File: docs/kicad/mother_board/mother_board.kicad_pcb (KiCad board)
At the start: 2 copper layers, 148 x 93 mm, 32 parts, among them J1 ROW_BOARDS, J10 PEDAL1, J11 PEDAL2, J12 PEDAL3, J13 PEDAL4, J14 GUITAR_IN, J15 LINE_OUT, J16 LEDS, J2 ROTARIES, J3 TE_DISPLAY, J4 RPI_DISPLAY, J5 rPi_5V, J6 RPI_RUN, J7 rpi_connector, J8 I2S_TXB, J9 EigthInchJack1, Q1 BC547, U1 teensyAudioRevD_WithAudio, U2 myTeensy4.1

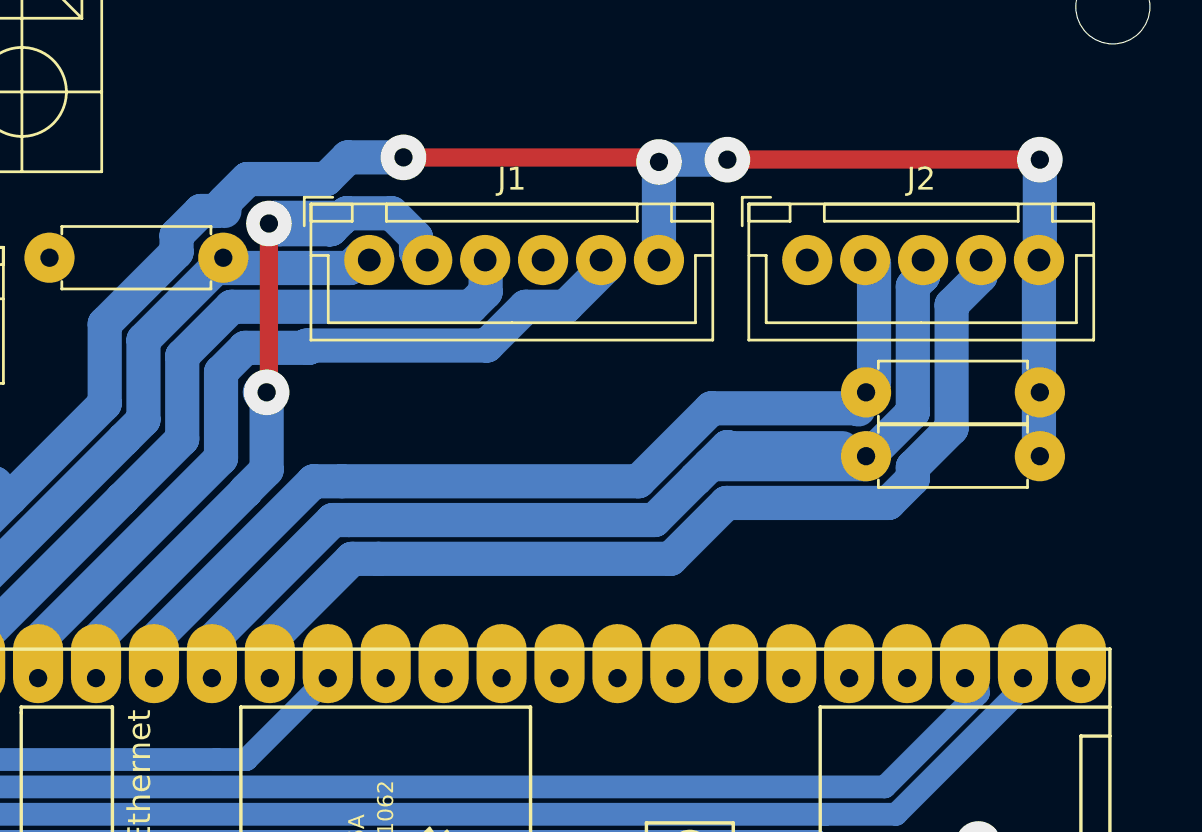
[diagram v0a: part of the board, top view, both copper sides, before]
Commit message: kicad changes to support actual Fusion 360 TE3 design efforts - created rotary board PCB
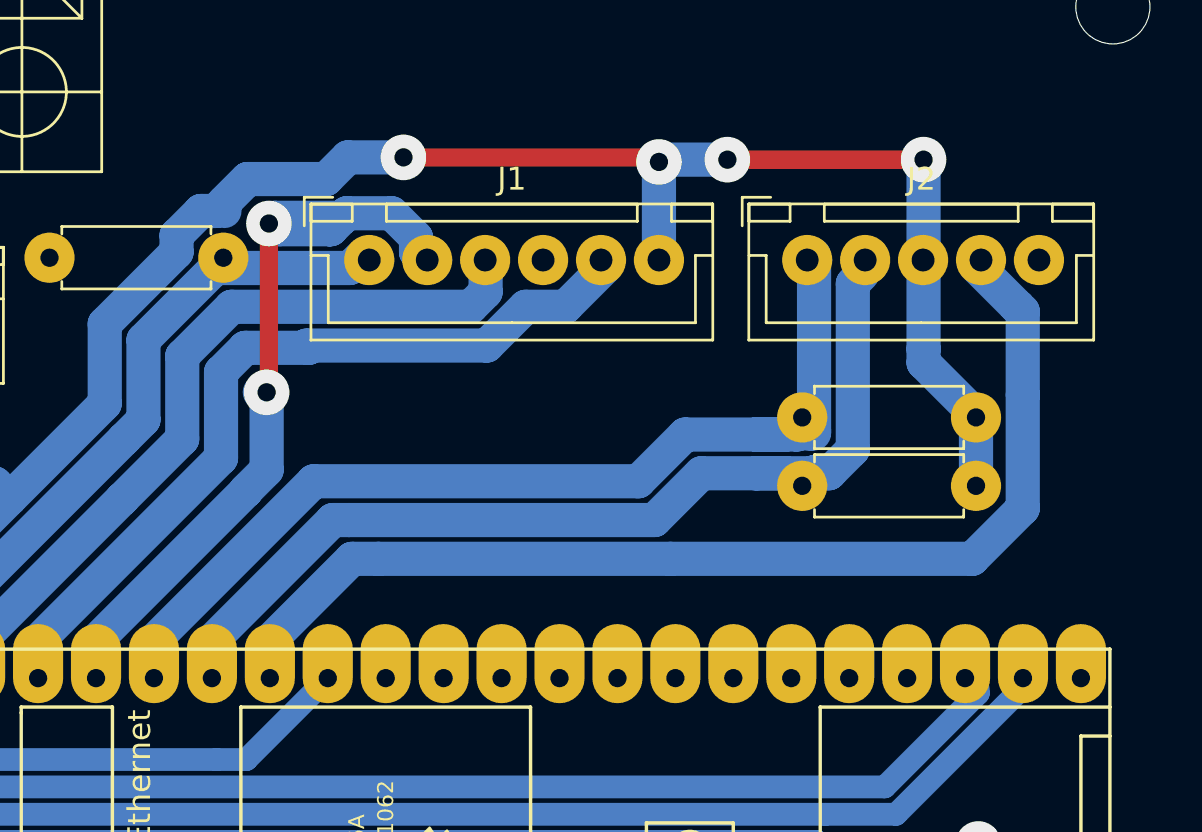
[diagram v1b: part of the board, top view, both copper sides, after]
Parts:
- moved R2 3.09 mm to (202.0, 84.0)
- moved R1 3.01 mm to (202.0, 81.0)
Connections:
- J2 pad 1: GND -> T41_SCL
- J2 pad 2: T41_SCL -> T41_SDA
- J2 pad 3: T41_SDA -> T41_3V3
- J2 pad 5: T41_3V3 -> GND
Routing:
- net ROT_INT: track 43.6 -> 51.1 mm
- net T41_SDA: track 50.3 -> 43.9 mm
- net T41_3V3: track 109.8 -> 107.0 mm
- net T41_SCL: track 42.6 -> 45.1 mm

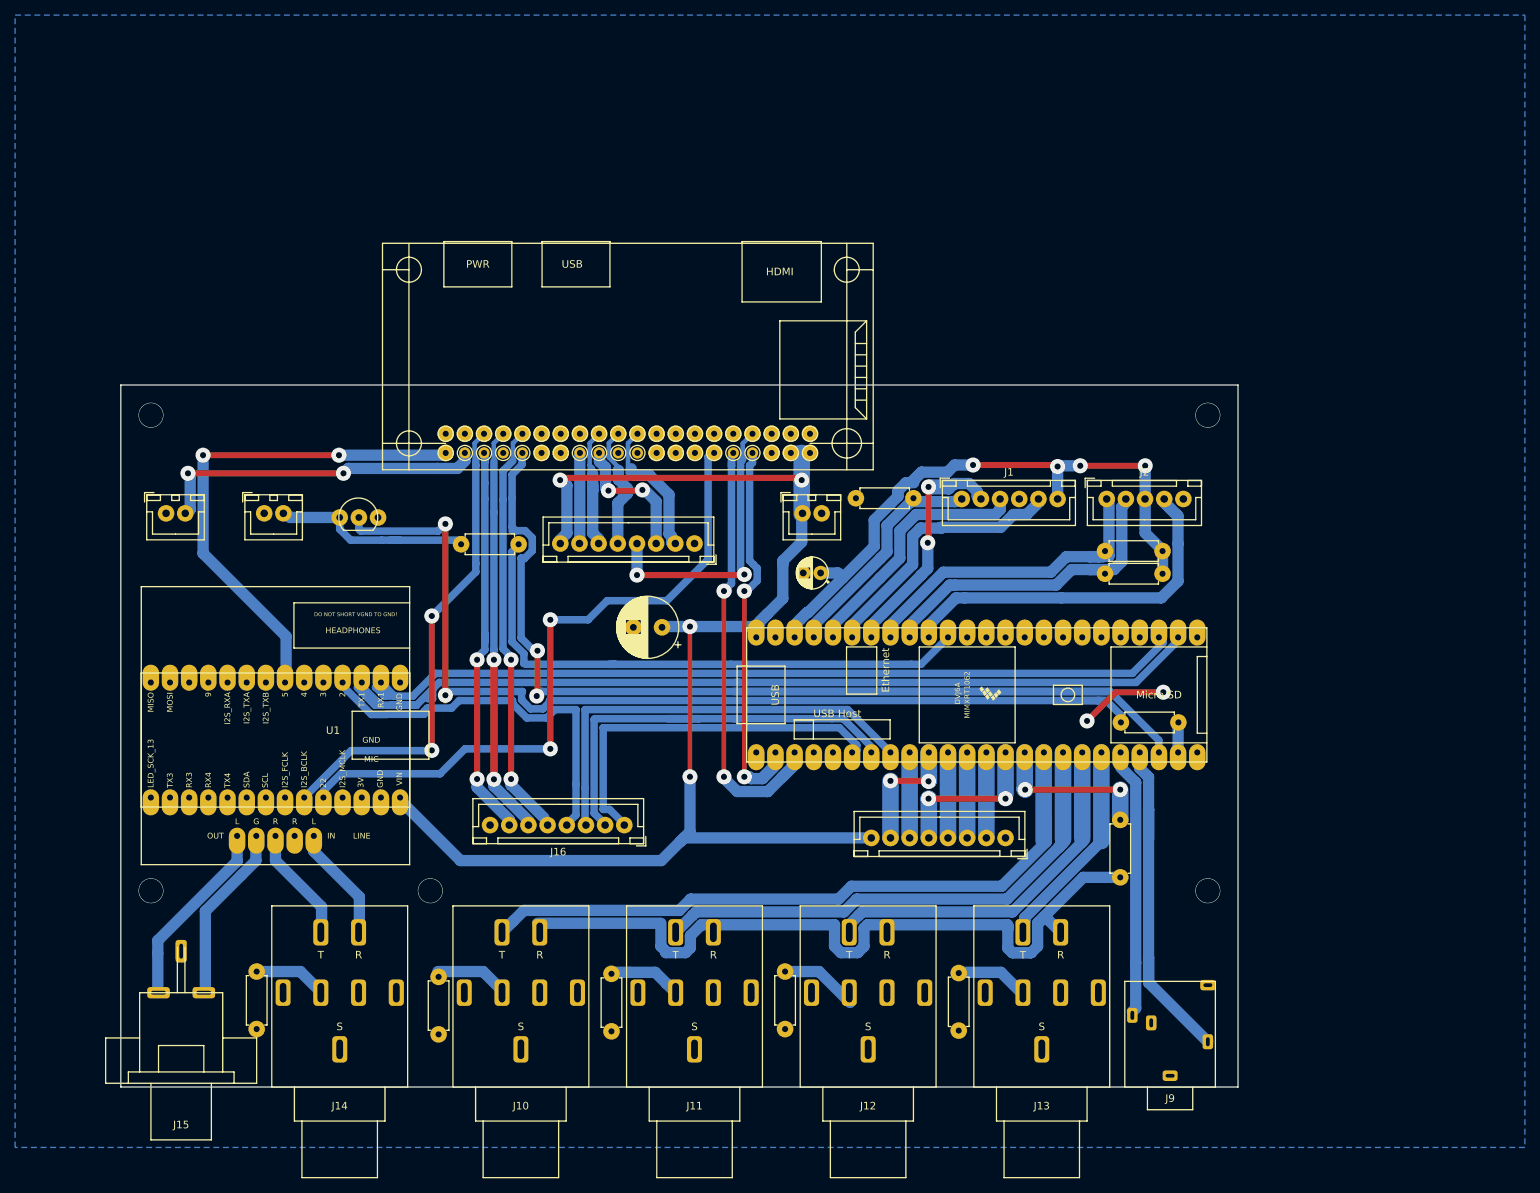
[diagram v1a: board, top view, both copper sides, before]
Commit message: added kicad led_board, updated mother board RCA socket
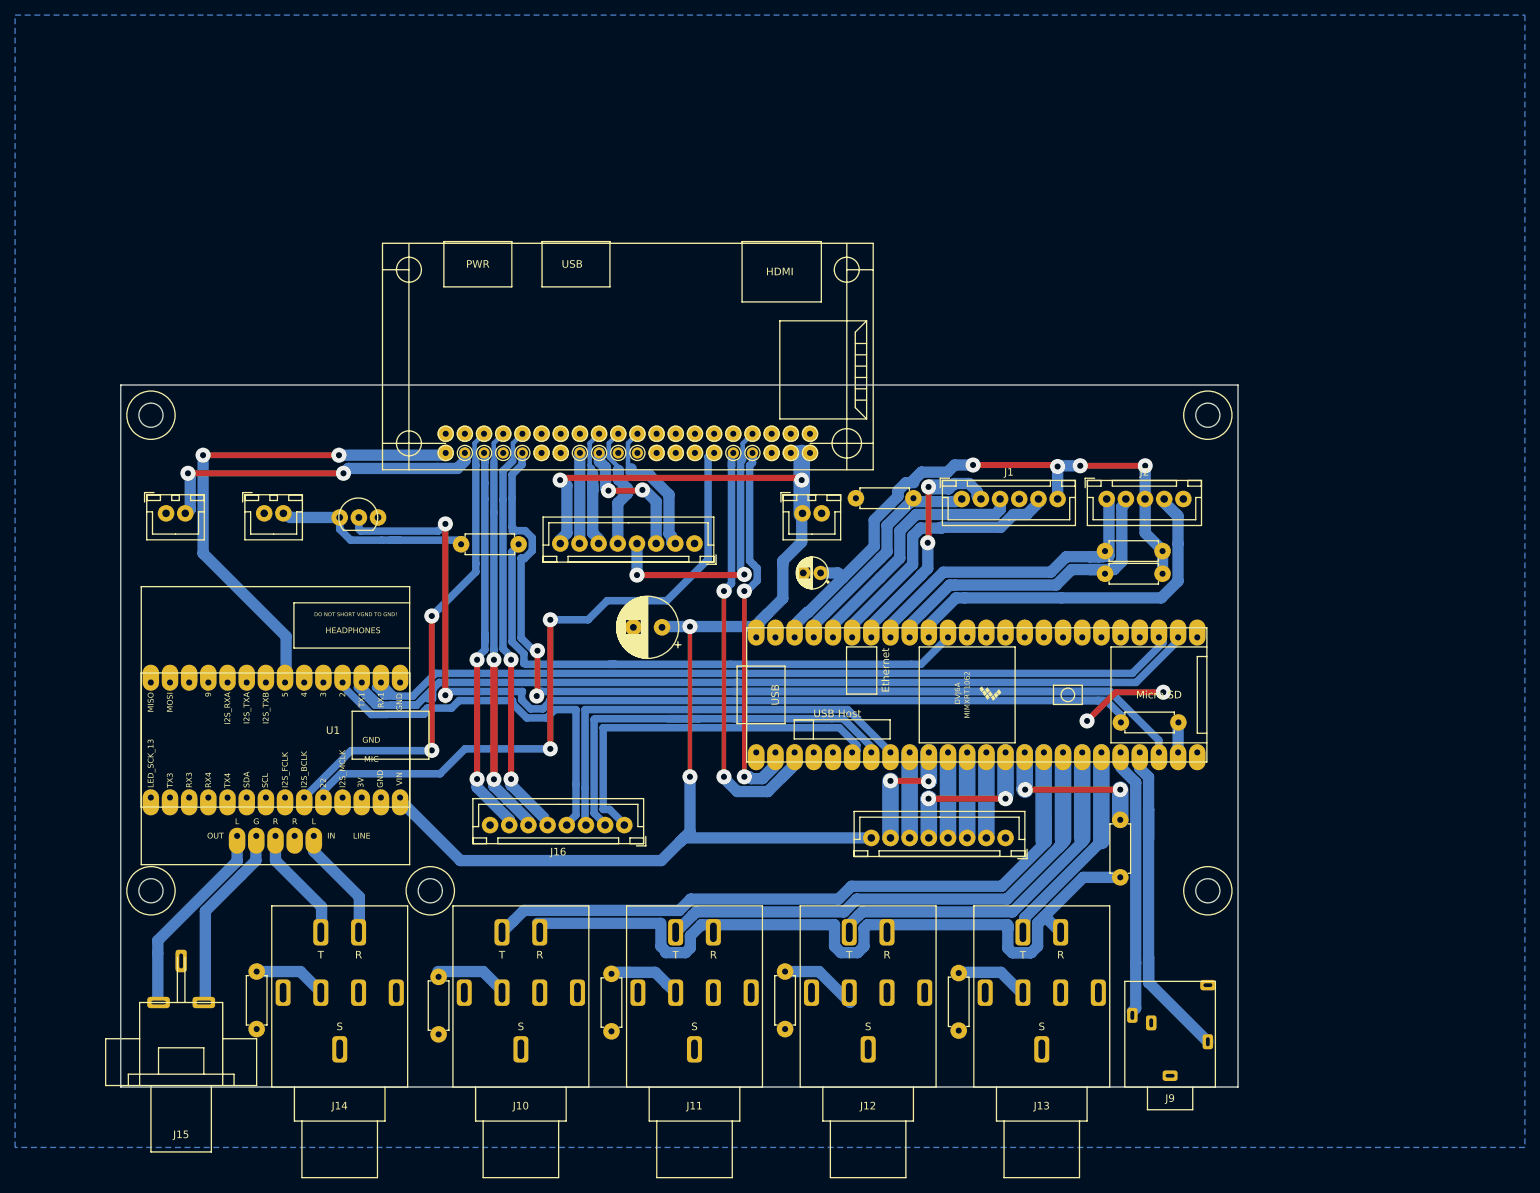
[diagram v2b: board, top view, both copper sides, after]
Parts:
- added REF**: myMountingHole_3.2mm_M3, 0_my_footprints:myMountingHole_3.2mm_M3, F.Cu at (68.0, 63.0)
- added REF**: myMountingHole_3.2mm_M3, 0_my_footprints:myMountingHole_3.2mm_M3, F.Cu at (68.0, 126.0)
- added REF**: myMountingHole_3.2mm_M3, 0_my_footprints:myMountingHole_3.2mm_M3, F.Cu at (105.0, 126.0)
- added REF**: myMountingHole_3.2mm_M3, 0_my_footprints:myMountingHole_3.2mm_M3, F.Cu at (208.0, 126.0)
- added REF**: myMountingHole_3.2mm_M3, 0_my_footprints:myMountingHole_3.2mm_M3, F.Cu at (208.0, 63.0)
- moved J15 1.30 mm to (72.0, 151.3)
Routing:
- net LINE_OUT_R: track 22.8 -> 24.1 mm
- net LINE_OUT_L: track 25.2 -> 26.3 mm
- net GND: vias 7 -> 2

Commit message: cutting actual TE3 milled circuit boards
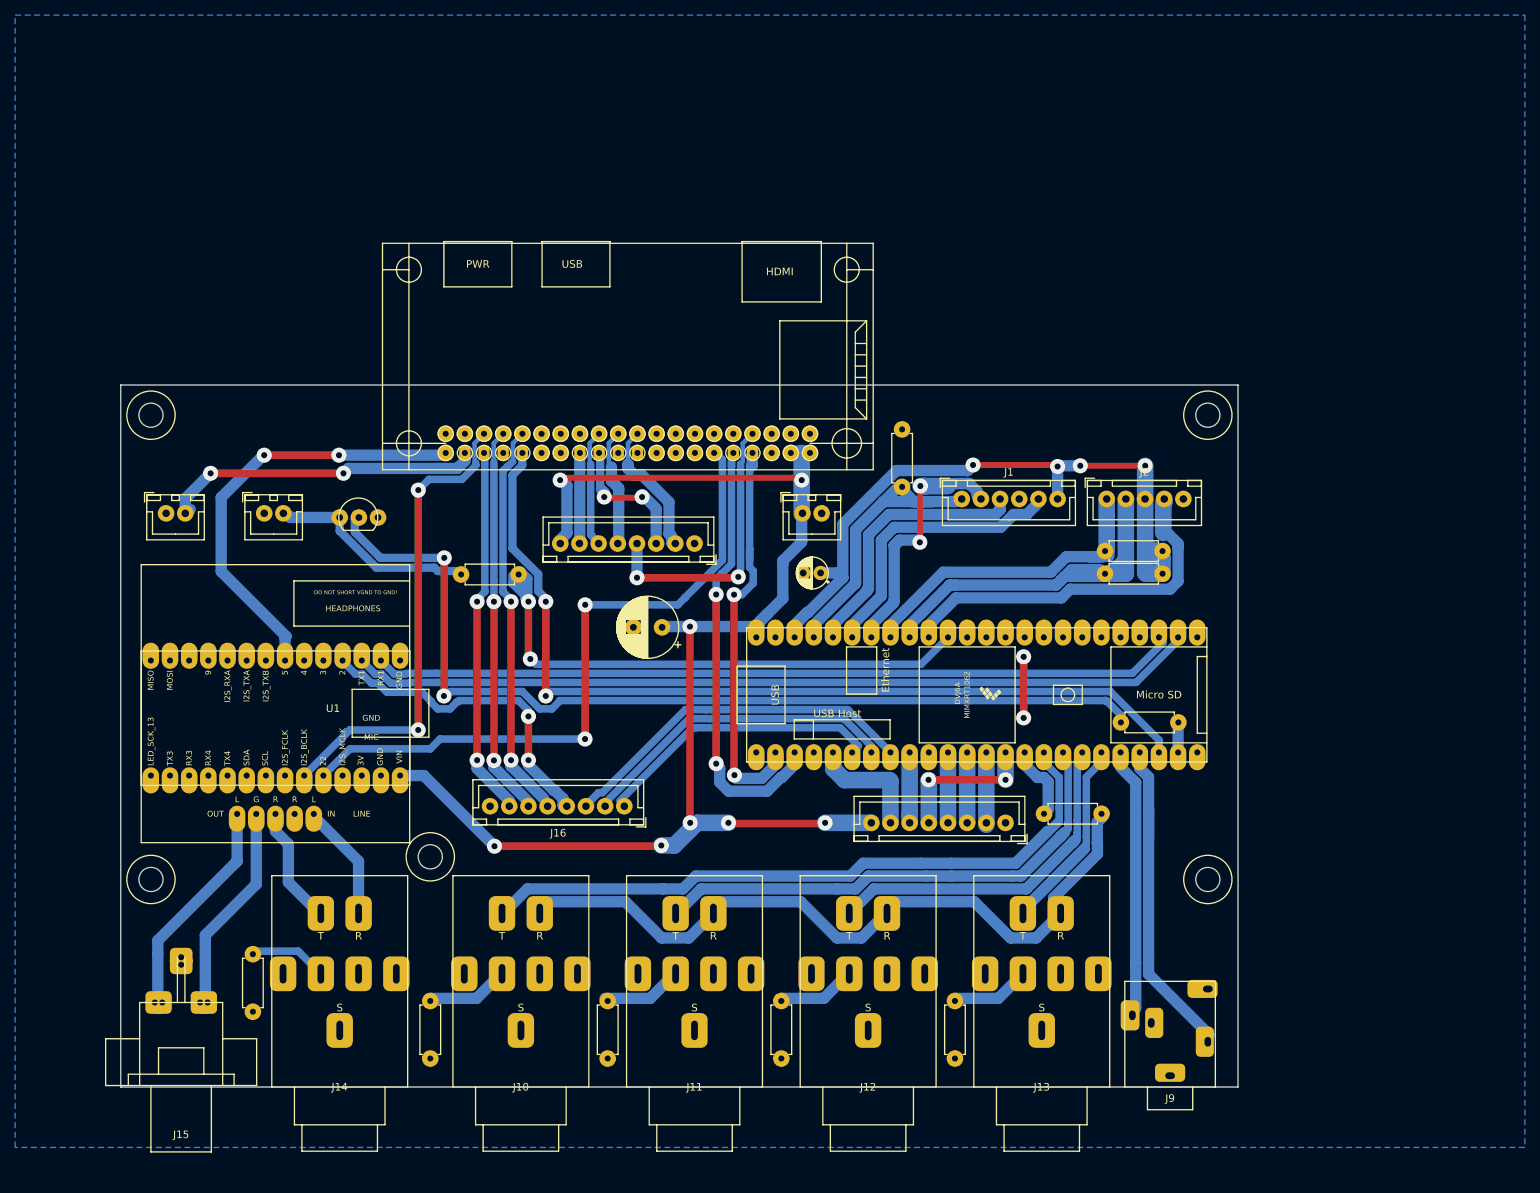
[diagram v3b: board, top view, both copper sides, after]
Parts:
- removed the REF** at (68.0, 126.0)
- removed the REF** at (105.0, 126.0)
- removed the REF** at (208.0, 126.0)
- added REF**: myMountingHole_3.2mm_M3, 0_my_footprints:myMountingHole_3.2mm_M3, F.Cu at (68.0, 124.5)
- added REF**: myMountingHole_3.2mm_M3, 0_my_footprints:myMountingHole_3.2mm_M3, F.Cu at (105.0, 121.5)
- added REF**: myMountingHole_3.2mm_M3, 0_my_footprints:myMountingHole_3.2mm_M3, F.Cu at (208.0, 124.5)
- moved R5 10.1 mm to (186.3, 115.8), turned to 0 degrees
- moved R3 4.00 mm to (116.7, 84.1)
- moved R8 3.93 mm to (151.5, 140.6)
- moved R9 3.73 mm to (174.5, 140.6)
- moved R7 3.63 mm to (128.5, 140.6)
- moved R6 3.38 mm to (105.0, 140.6)
- moved U1 2.91 mm to (101.0, 95.5)
- moved J10 2.50 mm to (117.0, 144.5)
- moved J11 2.50 mm to (140.0, 144.5)
- moved J12 2.50 mm to (163.0, 144.5)
- moved J13 2.50 mm to (186.0, 144.5)
- moved J14 2.50 mm to (93.0, 144.5)
- moved J16 2.50 mm to (130.7, 114.8)
- moved R10 2.35 mm to (81.5, 134.4)
- moved R11 2.12 mm to (167.5, 72.5), turned to 90 degrees
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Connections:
- U2 pad 10: T41_T_CS -> Net-(U2-Pad10)
- U2 pad 5: Net-(U2-Pad5) -> T41_T_CS
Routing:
- net RPI_READY: track 175.7 -> 120.3 mm
- net LED_RPI_RUN: track 58.1 -> 42.3 mm
- net Net-(J10-PadR): track 108.3 -> 95.5 mm
- net LED_T3_BUSY: track 50.2 -> 38.5 mm
- net BTN_SENSE: track 29.1 -> 39.8 mm
- net T41_RX8: track 122.3 -> 111.8 mm
- net LED_RPI_READY: track 57.8 -> 47.4 mm
- net I2S_RXB: track 66.2 -> 57.4 mm
- net LED_AUDIO_BUSY: track 51.3 -> 43.8 mm, vias 0 -> 2
- net Net-(Q1-Pad2): track 133.9 -> 126.6 mm
- net T41_SDA: track 43.9 -> 50.7 mm
- net PEDAL2: track 71.3 -> 65.8 mm
- net PEDAL3: track 50.3 -> 44.8 mm
- net LED_DIN: track 35.7 -> 40.7 mm
- net T41_TX8: track 111.3 -> 106.4 mm
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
